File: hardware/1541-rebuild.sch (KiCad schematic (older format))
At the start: 10 parts, among them IC1 ATMEGA1284P-P, P1 ISP, SW1 SW_PUSH, SW2 SW_PUSH, SW3 SW_PUSH, X1 20Mhz

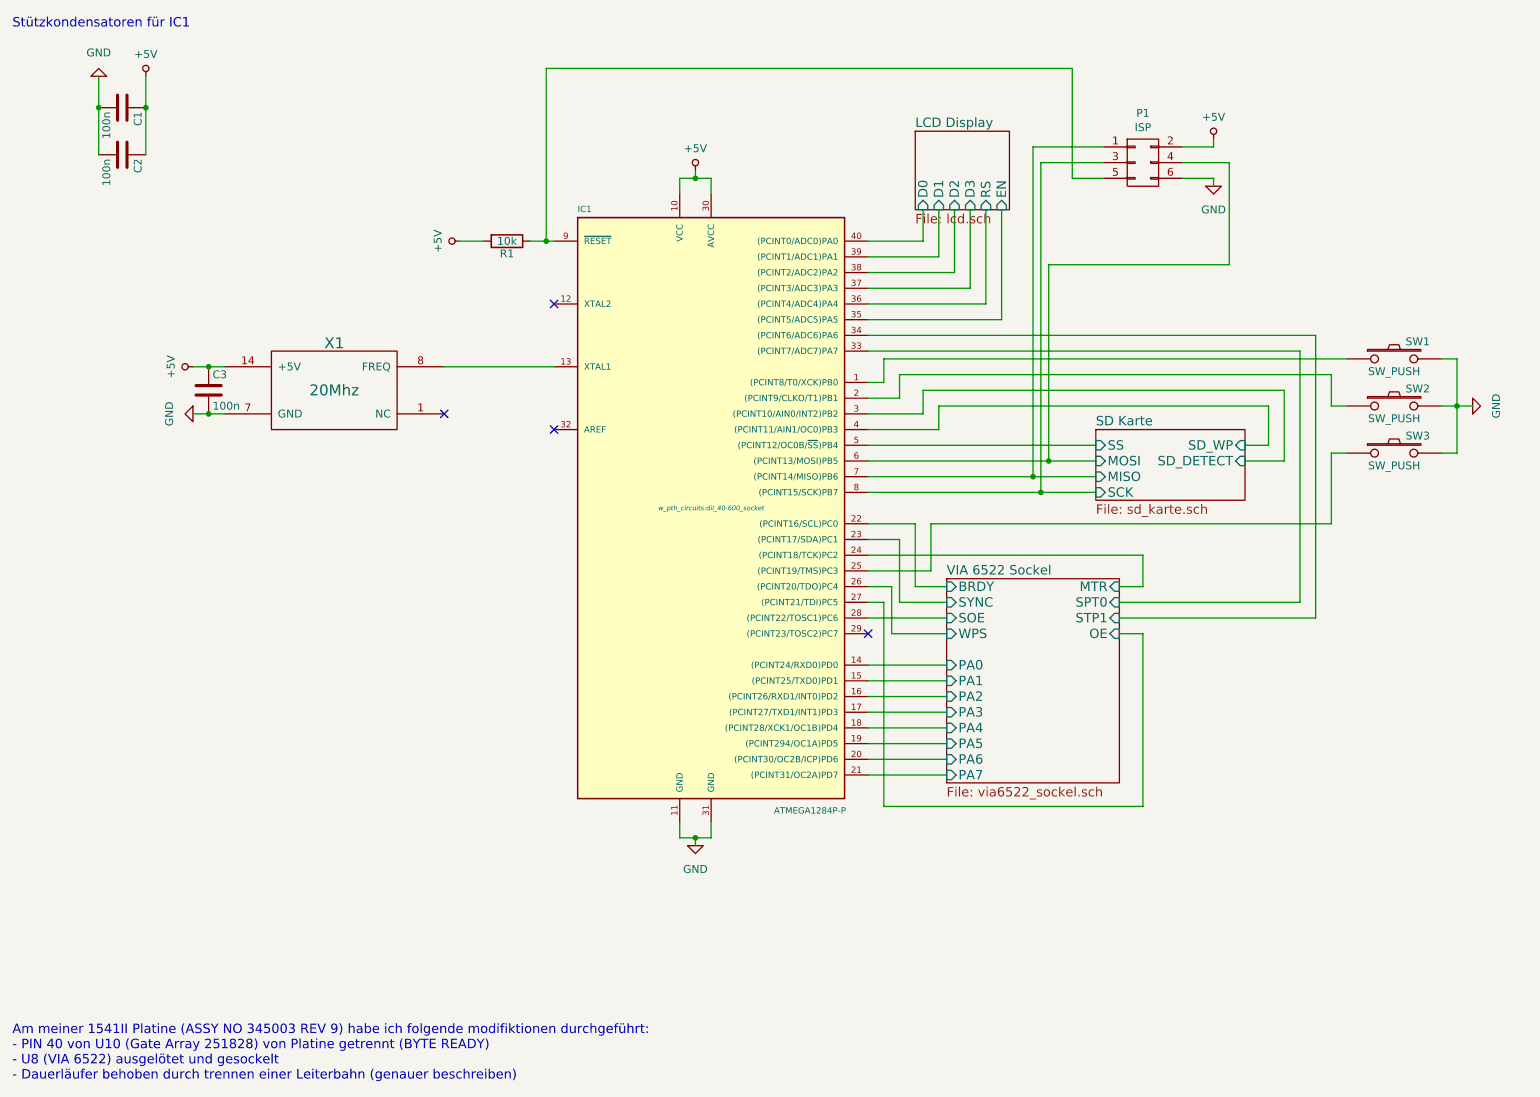
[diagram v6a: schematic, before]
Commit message: Debug LED im Schaltplan eingefügt.
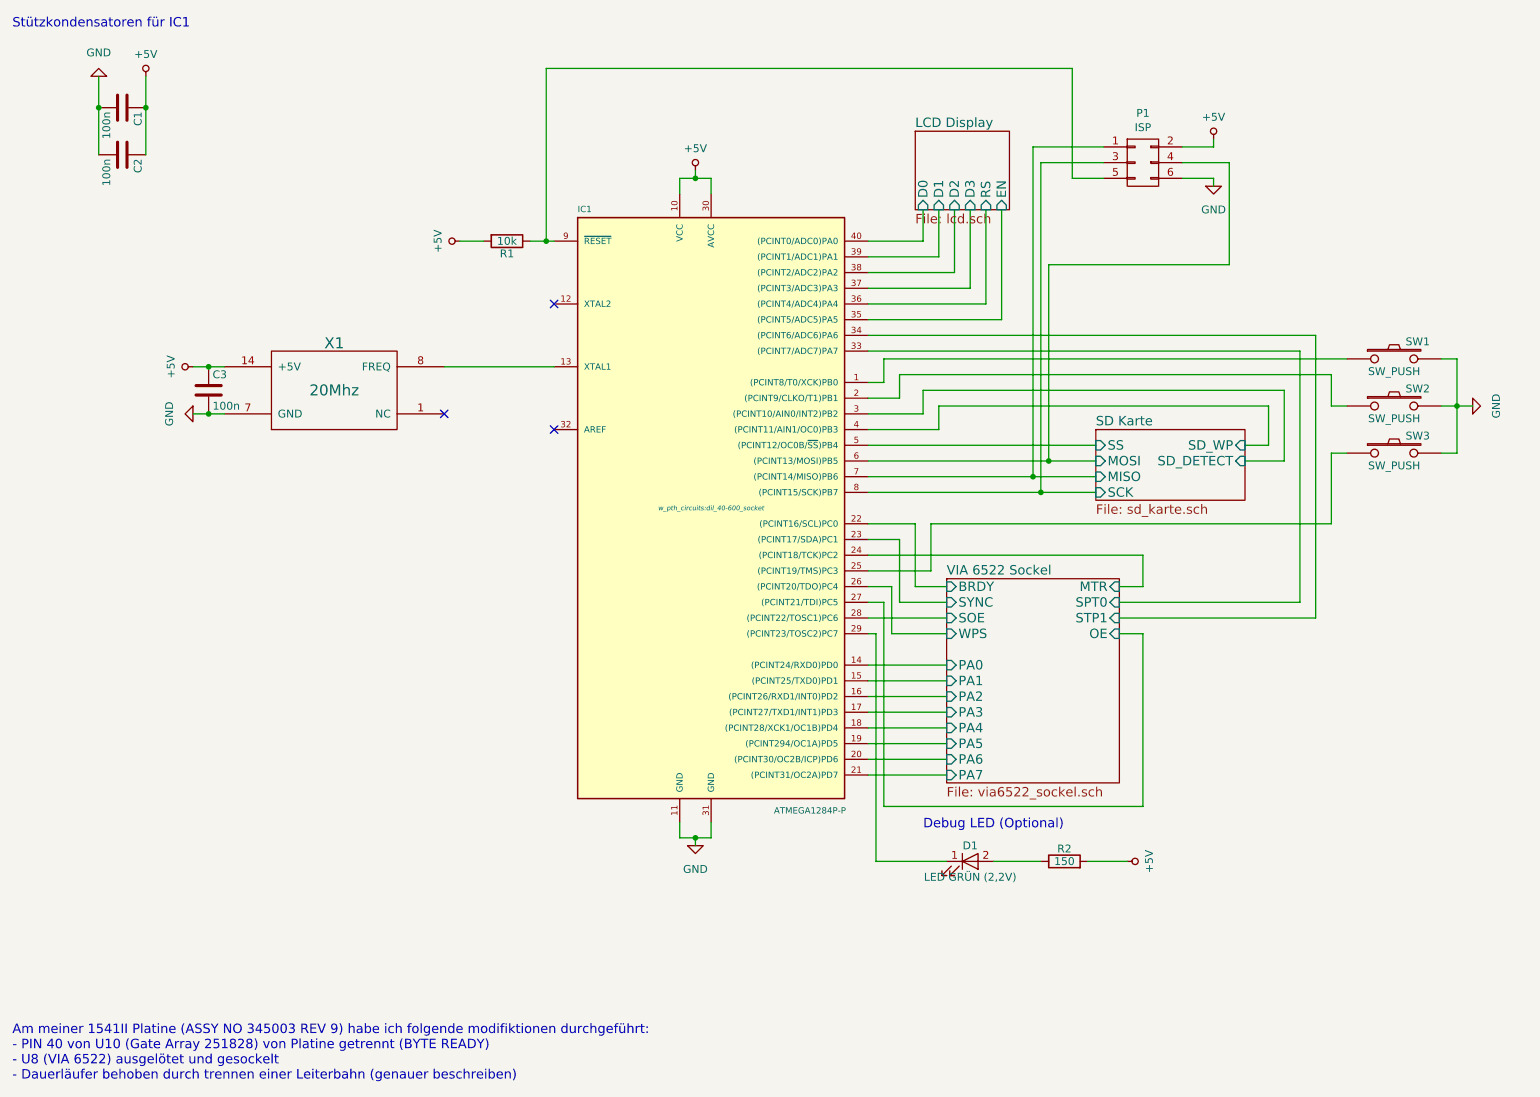
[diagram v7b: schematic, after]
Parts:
- added D1: LED GRÜN (2,2V), symbol LED
- added R2: 150, symbol R
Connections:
- net +5V: now also R2.2
- net at IC1.29 ((PCINT23/TOSC2)PC7): now also D1.1 (K)
- new net: D1.2 (A), R2.1
- no-connect marks 4 -> 3
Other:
- note added: "Debug LED (Optional)"
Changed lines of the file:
@@
 encoding utf-8
 Sheet 1 4
-Title "1541-rebuild"
-Date "2015-09-15"
-Rev "1.0"
+Title "1541-rebuid"
+Date "2018-04-18"
+Rev "1.1"
 Comp ""
 Comment1 "Erstellt: von: Thorsten Kattanek"
@@
 NoConn ~ 3400 3200
 $Comp
-L GND #PWR01
+L GND #PWR4
 U 1 1 55F7D4A6
 P 1800 3200
-F 0 "#PWR01" H 1800 2950 50  0001 C CNN
+F 0 "#PWR4" H 1800 2950 50  0001 C CNN
 F 1 "GND" H 1800 3050 50  0000 C CNN
 F 2 "" H 1800 3200 60  0000 C CNN
@@
 $EndComp
 $Comp
-L +5V #PWR02
+L +5V #PWR3
 U 1 1 55F7D4E4
 P 1800 2900
-F 0 "#PWR02" H 1800 2750 50  0001 C CNN
+F 0 "#PWR3" H 1800 2750 50  0001 C CNN
 F 1 "+5V" H 1800 3040 50  0000 C CNN
 F 2 "" H 1800 2900 60  0000 C CNN
@@
 NoConn ~ 4100 2500
 $Comp
-L GND #PWR03
+L GND #PWR7
 U 1 1 55F7EFD4
 P 5000 5950
-F 0 "#PWR03" H 5000 5700 50  0001 C CNN
+F 0 "#PWR7" H 5000 5700 50  0001 C CNN
 F 1 "GND" H 5000 5800 50  0000 C CNN
 F 2 "" H 5000 5950 60  0000 C CNN
@@
 $EndComp
 $Comp
-L +5V #PWR04
+L +5V #PWR6
 U 1 1 55F7F7C2
 P 5000 1650
-F 0 "#PWR04" H 5000 1500 50  0001 C CNN
+F 0 "#PWR6" H 5000 1500 50  0001 C CNN
 F 1 "+5V" H 5000 1790 50  0000 C CNN
 F 2 "" H 5000 1650 60  0000 C CNN
@@
 $EndComp
 $Comp
-L +5V #PWR05
+L +5V #PWR5
 U 1 1 55F7ED10
 P 3500 2100
-F 0 "#PWR05" H 3500 1950 50  0001 C CNN
+F 0 "#PWR5" H 3500 1950 50  0001 C CNN
 F 1 "+5V" H 3500 2240 50  0000 C CNN
 F 2 "" H 3500 2100 60  0000 C CNN
@@
 $EndComp
 $Comp
-L +5V #PWR06
+L +5V #PWR2
 U 1 1 55F800FF
 P 1500 1050
-F 0 "#PWR06" H 1500 900 50  0001 C CNN
+F 0 "#PWR2" H 1500 900 50  0001 C CNN
 F 1 "+5V" H 1500 1190 50  0000 C CNN
 F 2 "" H 1500 1050 60  0000 C CNN
@@
 $EndComp
 $Comp
-L GND #PWR07
+L GND #PWR1
 U 1 1 55F80221
 P 1200 1050
-F 0 "#PWR07" H 1200 800 50  0001 C CNN
+F 0 "#PWR1" H 1200 800 50  0001 C CNN
 F 1 "GND" H 1200 900 50  0000 C CNN
 F 2 "" H 1200 1050 60  0000 C CNN
@@
 F7 "EN" I B 6950 1900 60
 $EndSheet
-NoConn ~ 6100 4600
 $Sheet
 S 6600 4250 1100 1300
@@
 	3400 2900 4100 2900
 Wire Wire Line
-	1800 2900 2000 2900
+	1800 2900 1900 2900
+Wire Wire Line
+	1900 2900 2000 2900
 Connection ~ 1900 2900
 Wire Wire Line
-	1800 3200 2000 3200
+	1800 3200 1900 3200
+Wire Wire Line
+	1900 3200 2000 3200
 Connection ~ 1900 3200
 Wire Wire Line
 	4900 5800 4900 5900
 Wire Wire Line
-	4900 5900 5100 5900
+	4900 5900 5000 5900
+Wire Wire Line
+	5000 5900 5100 5900
 Wire Wire Line
 	5000 5900 5000 5950
@@
 	4900 1800 4900 1700
 Wire Wire Line
-	4900 1700 5100 1700
+	4900 1700 5000 1700
+Wire Wire Line
+	5000 1700 5100 1700
 Wire Wire Line
 	5000 1700 5000 1650
@@
 	3650 2100 3500 2100
 Wire Wire Line
-	3950 2100 4100 2100
-Wire Wire Line
-	1200 1050 1200 1550
+	3950 2100 4050 2100
+Wire Wire Line
+	4050 2100 4100 2100
+Wire Wire Line
+	1200 1050 1200 1250
+Wire Wire Line
+	1200 1250 1200 1550
 Connection ~ 1200 1250
 Wire Wire Line
-	1500 1050 1500 1550
+	1500 1050 1500 1250
+Wire Wire Line
+	1500 1250 1500 1550
 Connection ~ 1500 1250
 Wire Wire Line
@@
 	6100 3400 7550 3400
 Wire Wire Line
-	6100 3500 7550 3500
-Wire Wire Line
-	6100 3600 7550 3600
-Wire Wire Line
-	6100 3700 7550 3700
+	6100 3500 7250 3500
+Wire Wire Line
+	7250 3500 7550 3500
+Wire Wire Line
+	6100 3600 7150 3600
+Wire Wire Line
+	7150 3600 7550 3600
+Wire Wire Line
+	6100 3700 7200 3700
+Wire Wire Line
+	7200 3700 7550 3700
 Wire Wire Line
 	6100 3300 6550 3300
@@
 	9750 2850 9850 2850
 Wire Wire Line
-	9850 2850 9850 3450
-Wire Wire Line
-	9750 3150 9950 3150
+	9850 2850 9850 3150
+Wire Wire Line
+	9850 3150 9850 3450
+Wire Wire Line
+	9750 3150 9850 3150
+Wire Wire Line
+	9850 3150 9950 3150
 Connection ~ 9850 3150
 Wire Wire Line
@@
 	6200 4400 6100 4400
 $Comp
-L GND #PWR08
+L GND #PWR11
 U 1 1 57D3E94E
 P 9950 3150
-F 0 "#PWR08" H 9950 2900 50  0001 C CNN
+F 0 "#PWR11" H 9950 2900 50  0001 C CNN
 F 1 "GND" H 9950 3000 50  0000 C CNN
 F 2 "" H 9950 3150 60  0000 C CNN
@@
 Connection ~ 4050 2100
 $Comp
-L +5V #PWR09
+L +5V #PWR9
 U 1 1 58409984
 P 8300 1450
-F 0 "#PWR09" H 8300 1300 50  0001 C CNN
+F 0 "#PWR9" H 8300 1300 50  0001 C CNN
 F 1 "+5V" H 8300 1590 50  0000 C CNN
 F 2 "" H 8300 1450 60  0000 C CNN
@@
 	8300 1500 8300 1450
 $Comp
-L GND #PWR010
+L GND #PWR10
 U 1 1 58409C3B
 P 8300 1750
-F 0 "#PWR010" H 8300 1500 50  0001 C CNN
+F 0 "#PWR10" H 8300 1500 50  0001 C CNN
 F 1 "GND" H 8300 1600 50  0000 C CNN
 F 2 "" H 8300 1750 60  0000 C CNN
@@
 	7250 2250 7250 3500
 Connection ~ 7250 3500
+$Comp
+L LED D1
+U 1 1 5AD77D32
+P 6750 6050
+F 0 "D1" H 6750 6150 50  0000 C CNN
+F 1 "LED GRÜN (2,2V)" H 6750 5950 50  0000 C CNN
+F 2 "" H 6750 6050 50  0001 C CNN
+F 3 "" H 6750 6050 50  0001 C CNN
+	1    6750 6050
+	1    0    0    -1
+$EndComp
+Wire Wire Line
+	6150 4600 6150 6050
+Wire Wire Line
+	6150 4600 6100 4600
+$Comp
+L +5V #PWR8
+U 1 1 5AD79281
+P 7750 6050
+F 0 "#PWR8" H 7750 5900 50  0001 C CNN
+F 1 "+5V" H 7750 6190 50  0000 C CNN
+F 2 "" H 7750 6050 60  0000 C CNN
+F 3 "" H 7750 6050 60  0000 C CNN
+	1    7750 6050
+	0    1    1    0
+$EndComp
+Wire Wire Line
+	6150 6050 6600 6050
+Text Notes 6450 5850 0    60   ~ 0
+Debug LED (Optional)
+$Comp
+L R R2
+U 1 1 5AD7EF2D
+P 7350 6050
+F 0 "R2" V 7430 6050 50  0000 C CNN
+F 1 "150" V 7350 6050 50  0000 C CNN
+F 2 "" V 7280 6050 50  0001 C CNN
+F 3 "" H 7350 6050 50  0001 C CNN
+	1    7350 6050
+	0    -1   -1   0
+$EndComp
+Wire Wire Line
+	6900 6050 7200 6050
+Wire Wire Line
+	7500 6050 7750 6050
 $EndSCHEMATC

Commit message: Schaltplan angepasst. Reset kann optional per Jumper zwischen uController und Floppy Elektronik verbunden werden. Somit wird die Adapterplatine resettet wenn der C64 neu gestartet wird.
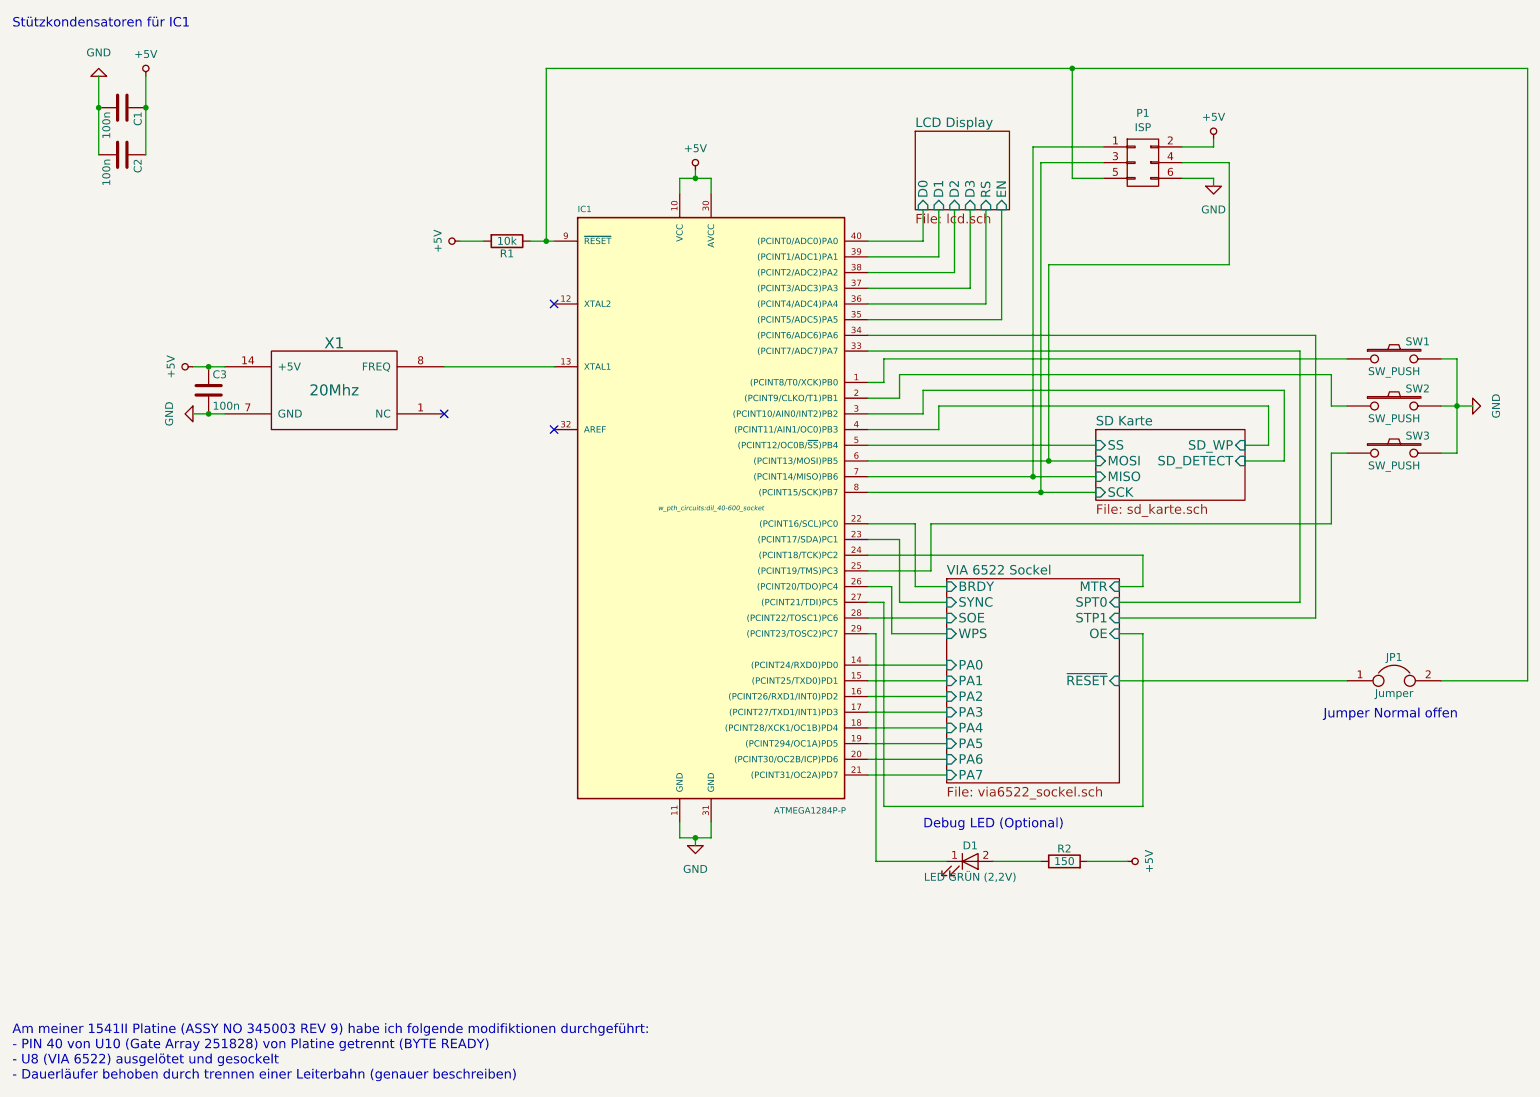
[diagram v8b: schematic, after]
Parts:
- added JP1: Jumper, symbol Jumper
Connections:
- net at IC1.9 (~RESET), P1.5 (P5), R1.1: now also JP1.2
- new net VIA 6522 Sockel/~RESET: JP1.1
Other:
- note added: "Jumper Normal offen"
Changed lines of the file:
@@
 F16 "MTR" I R 7700 4300 60
 F17 "WPS" I L 6600 4600 60
+F18 "~RESET" I R 7700 4900 60
 $EndSheet
 $Comp
@@
 	3400 2900 4100 2900
 Wire Wire Line
-	1800 2900 1900 2900
-Wire Wire Line
-	1900 2900 2000 2900
+	1800 2900 2000 2900
 Connection ~ 1900 2900
 Wire Wire Line
-	1800 3200 1900 3200
-Wire Wire Line
-	1900 3200 2000 3200
+	1800 3200 2000 3200
 Connection ~ 1900 3200
 Wire Wire Line
 	4900 5800 4900 5900
 Wire Wire Line
-	4900 5900 5000 5900
-Wire Wire Line
-	5000 5900 5100 5900
+	4900 5900 5100 5900
 Wire Wire Line
 	5000 5900 5000 5950
@@
 	4900 1800 4900 1700
 Wire Wire Line
-	4900 1700 5000 1700
-Wire Wire Line
-	5000 1700 5100 1700
+	4900 1700 5100 1700
 Wire Wire Line
 	5000 1700 5000 1650
@@
 	3650 2100 3500 2100
 Wire Wire Line
-	3950 2100 4050 2100
-Wire Wire Line
-	4050 2100 4100 2100
-Wire Wire Line
-	1200 1050 1200 1250
-Wire Wire Line
-	1200 1250 1200 1550
+	3950 2100 4100 2100
+Wire Wire Line
+	1200 1050 1200 1550
 Connection ~ 1200 1250
 Wire Wire Line
-	1500 1050 1500 1250
-Wire Wire Line
-	1500 1250 1500 1550
+	1500 1050 1500 1550
 Connection ~ 1500 1250
 Wire Wire Line
@@
 	6100 3400 7550 3400
 Wire Wire Line
-	6100 3500 7250 3500
-Wire Wire Line
-	7250 3500 7550 3500
-Wire Wire Line
-	6100 3600 7150 3600
-Wire Wire Line
-	7150 3600 7550 3600
-Wire Wire Line
-	6100 3700 7200 3700
-Wire Wire Line
-	7200 3700 7550 3700
+	6100 3500 7550 3500
+Wire Wire Line
+	6100 3600 7550 3600
+Wire Wire Line
+	6100 3700 7550 3700
 Wire Wire Line
 	6100 3300 6550 3300
@@
 	9750 2850 9850 2850
 Wire Wire Line
-	9850 2850 9850 3150
-Wire Wire Line
-	9850 3150 9850 3450
-Wire Wire Line
-	9750 3150 9850 3150
-Wire Wire Line
-	9850 3150 9950 3150
+	9850 2850 9850 3450
+Wire Wire Line
+	9750 3150 9950 3150
 Connection ~ 9850 3150
 Wire Wire Line
@@
 	4050 2100 4050 1000
 Wire Wire Line
-	4050 1000 7400 1000
+	4050 1000 10300 1000
 Wire Wire Line
 	7400 1000 7400 1700
@@
 Wire Wire Line
 	7500 6050 7750 6050
+Wire Wire Line
+	10300 1000 10300 4900
+Connection ~ 7400 1000
+$Comp
+L Jumper JP1
+U 1 1 5AD7B09A
+P 9450 4900
+F 0 "JP1" H 9450 5050 50  0000 C CNN
+F 1 "Jumper" H 9450 4820 50  0000 C CNN
+F 2 "" H 9450 4900 50  0001 C CNN
+F 3 "" H 9450 4900 50  0001 C CNN
+	1    9450 4900
+	1    0    0    -1
+$EndComp
+Wire Wire Line
+	10300 4900 9750 4900
+Wire Wire Line
+	9150 4900 7700 4900
+Text Notes 9000 5150 0    60   ~ 0
+Jumper Normal offen
 $EndSCHEMATC
